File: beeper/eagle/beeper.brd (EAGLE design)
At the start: 29.2 x 39.8 mm, 32 parts, among them J4 ICSP, Q1 16MHz, T1 3904, U1 ATA6631, U2 ATMEGA328P

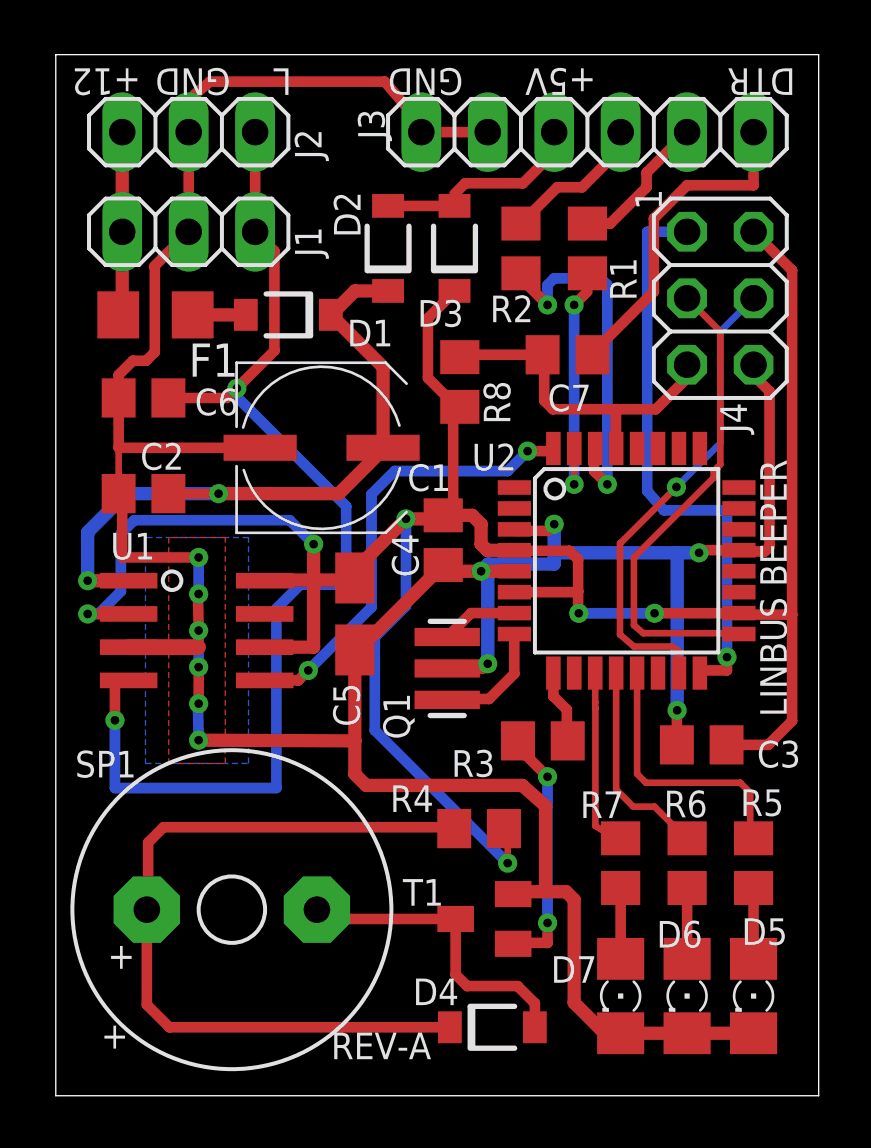
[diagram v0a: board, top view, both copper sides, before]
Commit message: Added ground plan on bottom layer. This version was uploaded to OSHPARK as version A.
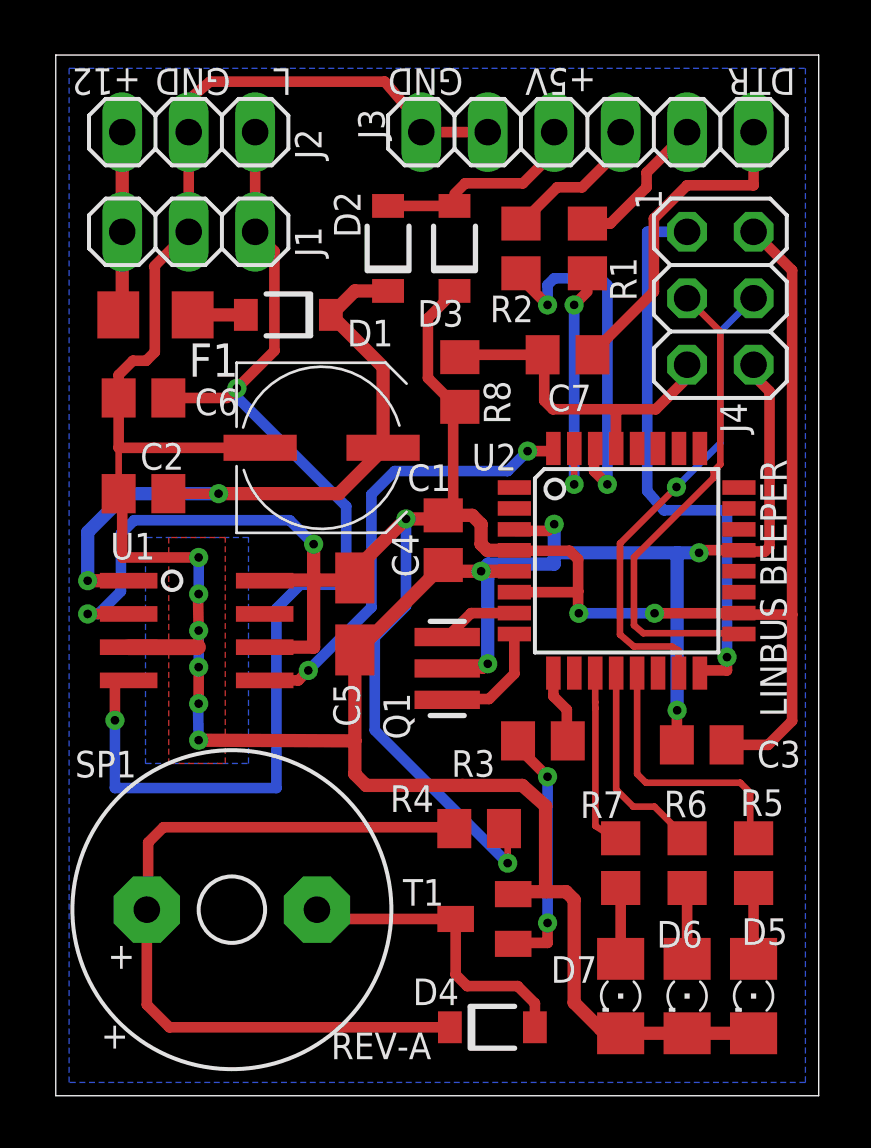
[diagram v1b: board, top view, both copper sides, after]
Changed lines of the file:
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@@
 <board>
 <plain>
-<wire x1="0" y1="0" x2="29.1594" y2="0" width="0" layer="20"/>
-<wire x1="29.1594" y1="0" x2="29.1594" y2="39.7918" width="0" layer="20"/>
-<wire x1="29.1594" y1="39.7918" x2="0" y2="39.7918" width="0" layer="20"/>
-<wire x1="0" y1="39.7918" x2="0" y2="0" width="0" layer="20"/>
+<wire x1="0" y1="0" x2="29.1592" y2="0" width="0" layer="20"/>
+<wire x1="29.1592" y1="0" x2="29.1592" y2="39.7764" width="0" layer="20"/>
+<wire x1="29.1592" y1="39.7764" x2="0" y2="39.7764" width="0" layer="20"/>
+<wire x1="0" y1="39.7764" x2="0" y2="0" width="0" layer="20"/>
 <text x="27.94" y="14.478" size="1.016" layer="21" rot="R90">LINBUS BEEPER</text>
 <text x="14.351" y="2.413" size="1.016" layer="21" rot="R180">REV-A</text>
@@
 <via x="23.749" y="14.732" extent="1-16" drill="0.3302"/>
 <wire x1="23.749" y1="14.732" x2="23.749" y2="20.7518" width="0.508" layer="16"/>
+<polygon width="0.254" layer="16" rank="6">
+<vertex x="0.508" y="39.2684"/>
+<vertex x="28.6512" y="39.2684"/>
+<vertex x="28.6512" y="0.508"/>
+<vertex x="0.508" y="0.508"/>
+</polygon>
 </signal>
 <signal name="N$2">

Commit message: Updated annotations of beeper schematic. No semantic changes.
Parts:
- F1: value 250ma -> 250ma Slow
- T1: value 3904 -> MMBT3904
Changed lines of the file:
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@@
 <attribute name="NAME" x="16.7894" y="13.208" size="1.016" layer="25" rot="R180"/>
 </element>
-<element name="T1" library="transistor" package="SOT23-BEC" value="3904" x="16.383" y="6.7564" smashed="yes" rot="R90">
+<element name="T1" library="transistor" package="SOT23-BEC" value="MMBT3904" x="16.383" y="6.7564" smashed="yes" rot="R90">
 <attribute name="NAME" x="14.8336" y="8.2804" size="1.016" layer="25" rot="R180"/>
 </element>
@@
 <attribute name="NAME" x="12.8524" y="21.4884" size="1.016" layer="25" rot="R270"/>
 </element>
-<element name="F1" library="beeper" package="1206" value="250ma" x="3.81" y="29.845" smashed="yes">
+<element name="F1" library="beeper" package="1206" value="250ma Slow" x="3.81" y="29.845" smashed="yes">
 <attribute name="NAME" x="5.08" y="27.4828" size="1.27" layer="25"/>
 </element>

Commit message: Refactoring the beeper schema. No semantic change.
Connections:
- net N$14 renamed SER_RX
- net N$15 renamed RESET
- net N$17 renamed BUZZER
- net N$20 renamed MOSI
- net N$22 renamed SER_TX
- net N$25 renamed MISO
- net N$28 renamed SCK
- net N$7 renamed ERROR_LED
- net N$8 renamed FRAME_LED
- net N$9 renamed STATUS_LED
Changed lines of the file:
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@@
 <wire x1="26.67" y1="7.94" x2="26.67" y2="5.232" width="0.4064" layer="1"/>
 </signal>
-<signal name="N$15">
+<signal name="RESET">
 <contactref element="J4" pad="5"/>
 <contactref element="C7" pad="2"/>
@@
 <wire x1="15.9156" y1="22.1844" x2="14.8082" y2="22.1844" width="0.508" layer="1"/>
 </signal>
-<signal name="N$14">
+<signal name="SER_RX">
 <contactref element="R2" pad="1"/>
 <contactref element="U2" pad="30"/>
@@
 <wire x1="21.59" y1="36.195" x2="21.59" y2="36.83" width="0.4064" layer="1"/>
 </signal>
-<signal name="N$22">
+<signal name="SER_TX">
 <contactref element="R1" pad="1"/>
 <contactref element="U2" pad="31"/>
@@
 <wire x1="15.24" y1="34.4678" x2="15.24" y2="34.01" width="0.254" layer="1"/>
 </signal>
-<signal name="N$20">
+<signal name="MOSI">
 <contactref element="J4" pad="4"/>
 <contactref element="U2" pad="15"/>
@@
 <wire x1="25.4" y1="29.21" x2="26.67" y2="30.48" width="0.254" layer="16"/>
 </signal>
-<signal name="N$25">
+<signal name="MISO">
 <contactref element="J4" pad="1"/>
 <contactref element="U2" pad="16"/>
@@
 <via x="25.654" y="16.764" extent="1-16" drill="0.3302"/>
 </signal>
-<signal name="N$28">
+<signal name="SCK">
 <contactref element="J4" pad="3"/>
 <contactref element="U2" pad="17"/>
@@
 <wire x1="25.908" y1="17.6784" x2="26.1112" y2="17.647" width="0.254" layer="1"/>
 </signal>
-<signal name="N$7">
+<signal name="ERROR_LED">
 <contactref element="R5" pad="2"/>
 <contactref element="U2" pad="13"/>
@@
 <wire x1="22.2186" y1="12.3" x2="22.2186" y2="16.1544" width="0.254" layer="1"/>
 </signal>
-<signal name="N$8">
+<signal name="FRAME_LED">
 <contactref element="R6" pad="2"/>
 <contactref element="U2" pad="12"/>
@@
 <wire x1="21.4186" y1="11.703" x2="21.4186" y2="16.1544" width="0.254" layer="1"/>
 </signal>
-<signal name="N$9">
+<signal name="STATUS_LED">
 <contactref element="R7" pad="2"/>
 <contactref element="U2" pad="11"/>
@@
 <wire x1="15.283" y1="4.6306" x2="15.283" y2="6.7564" width="0.4064" layer="1"/>
 </signal>
-<signal name="N$17">
+<signal name="BUZZER">
 <contactref element="R3" pad="1"/>
 <contactref element="U2" pad="9"/>

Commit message: Added '40V' annotation to VBAT capacitor.
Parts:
- C1: value 22uF -> 22uF 40V
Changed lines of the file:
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@@
 <attribute name="NAME" x="18.923" y="4.318" size="1.016" layer="25"/>
 </element>
-<element name="C1" library="rcl" package="UD-6,3X5,8_NICHICON" value="22uF" x="10.16" y="24.765" smashed="yes">
+<element name="C1" library="rcl" package="UD-6,3X5,8_NICHICON" value="22uF 40V" x="10.16" y="24.765" smashed="yes">
 <attribute name="NAME" x="13.4366" y="23.114" size="1.016" layer="25"/>
 </element>

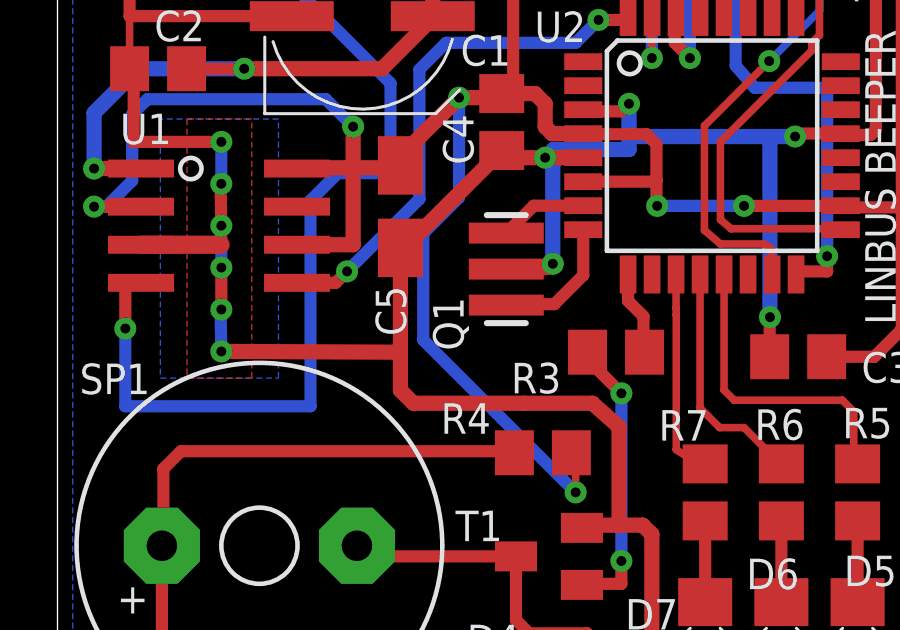
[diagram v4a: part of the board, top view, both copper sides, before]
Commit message: Minor text changes in beeper schematic. No semantic change.
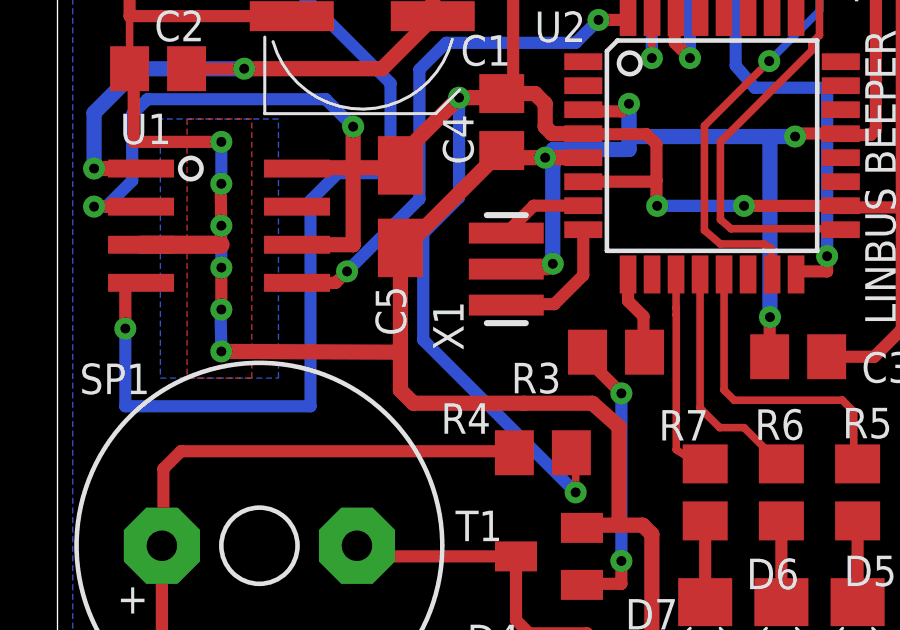
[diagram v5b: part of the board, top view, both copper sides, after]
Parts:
- renumbered Q1 to X1
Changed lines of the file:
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@@
 <attribute name="NAME" x="15.5862" y="30.4104" size="1.016" layer="25" rot="R180"/>
 </element>
-<element name="Q1" library="beeper" package="RESONATOR-SMD" value="16MHz" x="14.9606" y="16.3322" smashed="yes" rot="R90">
+<element name="X1" library="beeper" package="RESONATOR-SMD" value="16MHz" x="14.9606" y="16.3322" smashed="yes" rot="R90">
 <attribute name="NAME" x="13.5382" y="13.6144" size="1.016" layer="25" rot="R90"/>
 </element>
@@
 <contactref element="J4" pad="6"/>
 <contactref element="T1" pad="E"/>
-<contactref element="Q1" pad="2"/>
+<contactref element="X1" pad="2"/>
 <contactref element="D5" pad="C"/>
 <contactref element="D6" pad="C"/>
@@
 <signal name="XTAL1">
 <contactref element="U2" pad="7"/>
-<contactref element="Q1" pad="3"/>
+<contactref element="X1" pad="3"/>
 <wire x1="17.526" y1="18.447" x2="15.8754" y2="18.447" width="0.4064" layer="1"/>
 <wire x1="15.8754" y1="18.447" x2="14.9606" y2="17.5322" width="0.4064" layer="1"/>
 </signal>
 <signal name="XTAL2">
-<contactref element="Q1" pad="1"/>
+<contactref element="X1" pad="1"/>
 <contactref element="U2" pad="8"/>
 <wire x1="14.9606" y1="15.1322" x2="15.1322" y2="15.1322" width="0.254" layer="1"/>

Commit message: Tweaked beeper resistor values. No schema or layout change.
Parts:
- C7: value 0.01uF -> 0.1uF
- D4: value MBR0560 -> MBR0540
- R3: value 5K -> 3.3K
- R4: value 220 -> 0
- R6, R7: value 470 -> 3.3K
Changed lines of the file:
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@@
 <attribute name="NAME" x="26.162" y="10.6934" size="1.016" layer="25"/>
 </element>
-<element name="R6" library="rcl" package="R0805" value="470" x="24.13" y="8.89" smashed="yes" rot="R90">
+<element name="R6" library="rcl" package="R0805" value="3.3K" x="24.13" y="8.89" smashed="yes" rot="R90">
 <attribute name="NAME" x="23.241" y="10.6426" size="1.016" layer="25"/>
 </element>
-<element name="R7" library="rcl" package="R0805" value="470" x="21.59" y="8.89" smashed="yes" rot="R90">
+<element name="R7" library="rcl" package="R0805" value="3.3K" x="21.59" y="8.89" smashed="yes" rot="R90">
 <attribute name="NAME" x="20.0406" y="10.6172" size="1.016" layer="25"/>
 </element>
@@
 <attribute name="NAME" x="28.4734" y="13.5636" size="1.016" layer="25" rot="R180"/>
 </element>
-<element name="C7" library="rcl" package="C0805" value="0.01uF" x="19.558" y="28.321" smashed="yes" rot="R180">
+<element name="C7" library="rcl" package="C0805" value="0.1uF" x="19.558" y="28.321" smashed="yes" rot="R180">
 <attribute name="NAME" x="20.4724" y="27.178" size="1.016" layer="25" rot="R180"/>
 </element>
@@
 <attribute name="NAME" x="25.4" y="26.4922" size="1.016" layer="25" ratio="10" rot="R270"/>
 </element>
-<element name="R3" library="rcl" package="R0805" value="5K" x="18.6182" y="13.5636" smashed="yes" rot="R180">
+<element name="R3" library="rcl" package="R0805" value="3.3K" x="18.6182" y="13.5636" smashed="yes" rot="R180">
 <attribute name="NAME" x="16.7894" y="13.208" size="1.016" layer="25" rot="R180"/>
 </element>
@@
 <attribute name="NAME" x="14.8336" y="8.2804" size="1.016" layer="25" rot="R180"/>
 </element>
-<element name="R4" library="rcl" package="R0805" value="220" x="16.1798" y="10.2108" smashed="yes">
+<element name="R4" library="rcl" package="R0805" value="0" x="16.1798" y="10.2108" smashed="yes">
 <attribute name="NAME" x="12.7762" y="10.8458" size="1.016" layer="25"/>
 </element>
@@
 <attribute name="NAME" x="0.7366" y="12.1666" size="1.016" layer="25" ratio="10"/>
 </element>
-<element name="D4" library="diode" package="SOD123FL" value="MBR0560" x="16.6878" y="2.6162" smashed="yes">
+<element name="D4" library="diode" package="SOD123FL" value="MBR0540" x="16.6878" y="2.6162" smashed="yes">
 <attribute name="NAME" x="13.6464" y="3.4638" size="1.016" layer="25"/>
 </element>
